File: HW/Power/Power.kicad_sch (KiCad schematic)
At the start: 7 parts, among them J1 Battery, J2 Source, U1 L7805

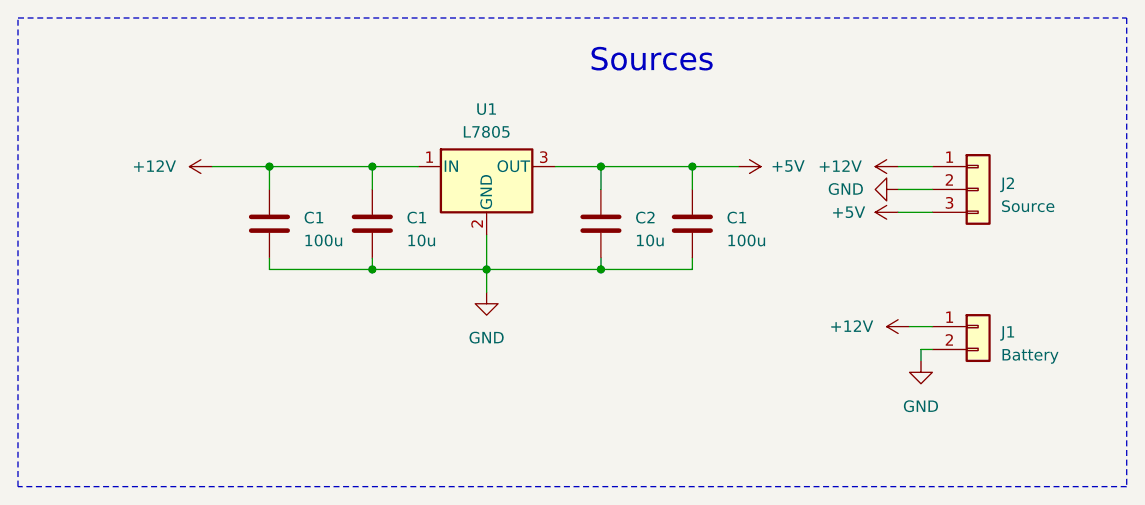
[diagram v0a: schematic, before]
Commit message: PCB's OK: power, H Bridge driver
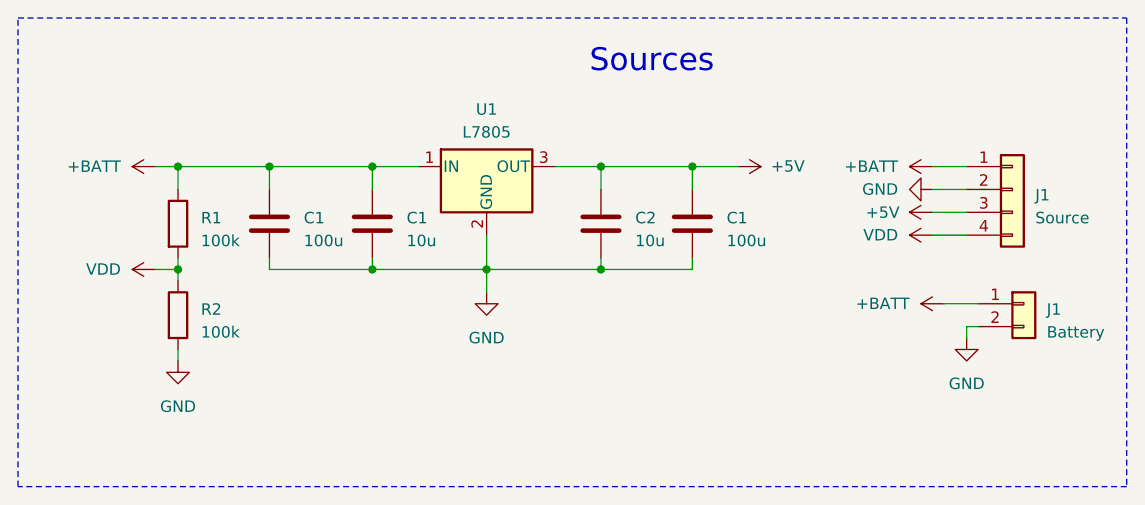
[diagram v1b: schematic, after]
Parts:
- removed J2: Source, Connector_PinHeader_2.54mm:PinHeader_1x03_P2.54mm_Vertical, symbol Connector_Generic:Conn_01x03
- added J1: Source, Connector_PinHeader_2.54mm:PinHeader_1x04_P2.54mm_Vertical, symbol Connector_Generic:Conn_01x04
- added R1, R2: 100k, Resistor_THT:R_Axial_DIN0204_L3.6mm_D1.6mm_P7.62mm_Horizontal, symbol Device:R
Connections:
- net +5V: now also J1.3 (Pin_3)
- net GND: now also J1.2 (Pin_2), R2.2
- net +12V renamed +BATT
- net +BATT: now also J1.1 (Pin_1), R1.1
- new net VDD: J1.4 (Pin_4), R1.2, R2.1
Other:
- moved on the sheet: J1
